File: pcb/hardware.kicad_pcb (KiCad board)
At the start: 4 copper layers, 174 parts, among them J1 Micro_SD_Card_Det_Hirose_DM3AT, J2 USB_A, J3 USB_A, U1 AS4C512M16D3L-12BIN, U2 A33, U3 TPS62095RGTR, U4 TPS62095RGTR, U5 TPS62095RGTR, U6 TPS62095RGTR, U7 AP131-25, U8 MPM-15-5, Y1 24Mhz, Y2 32.768khz

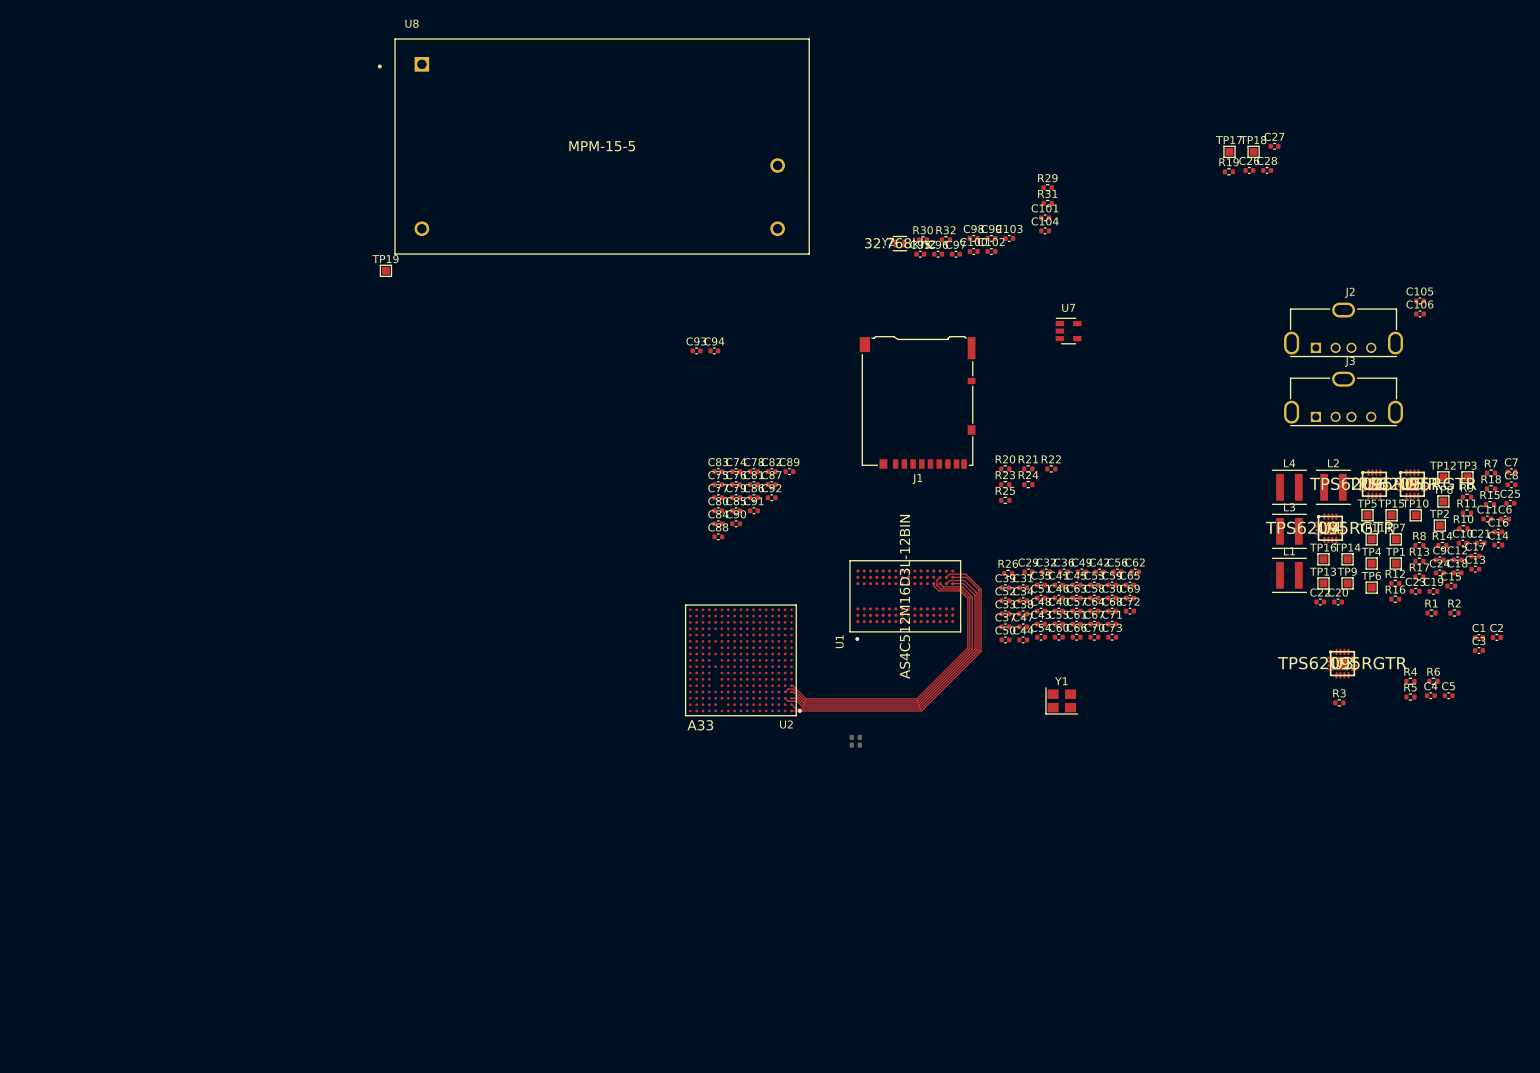
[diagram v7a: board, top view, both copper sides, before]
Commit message: RAM hooked up
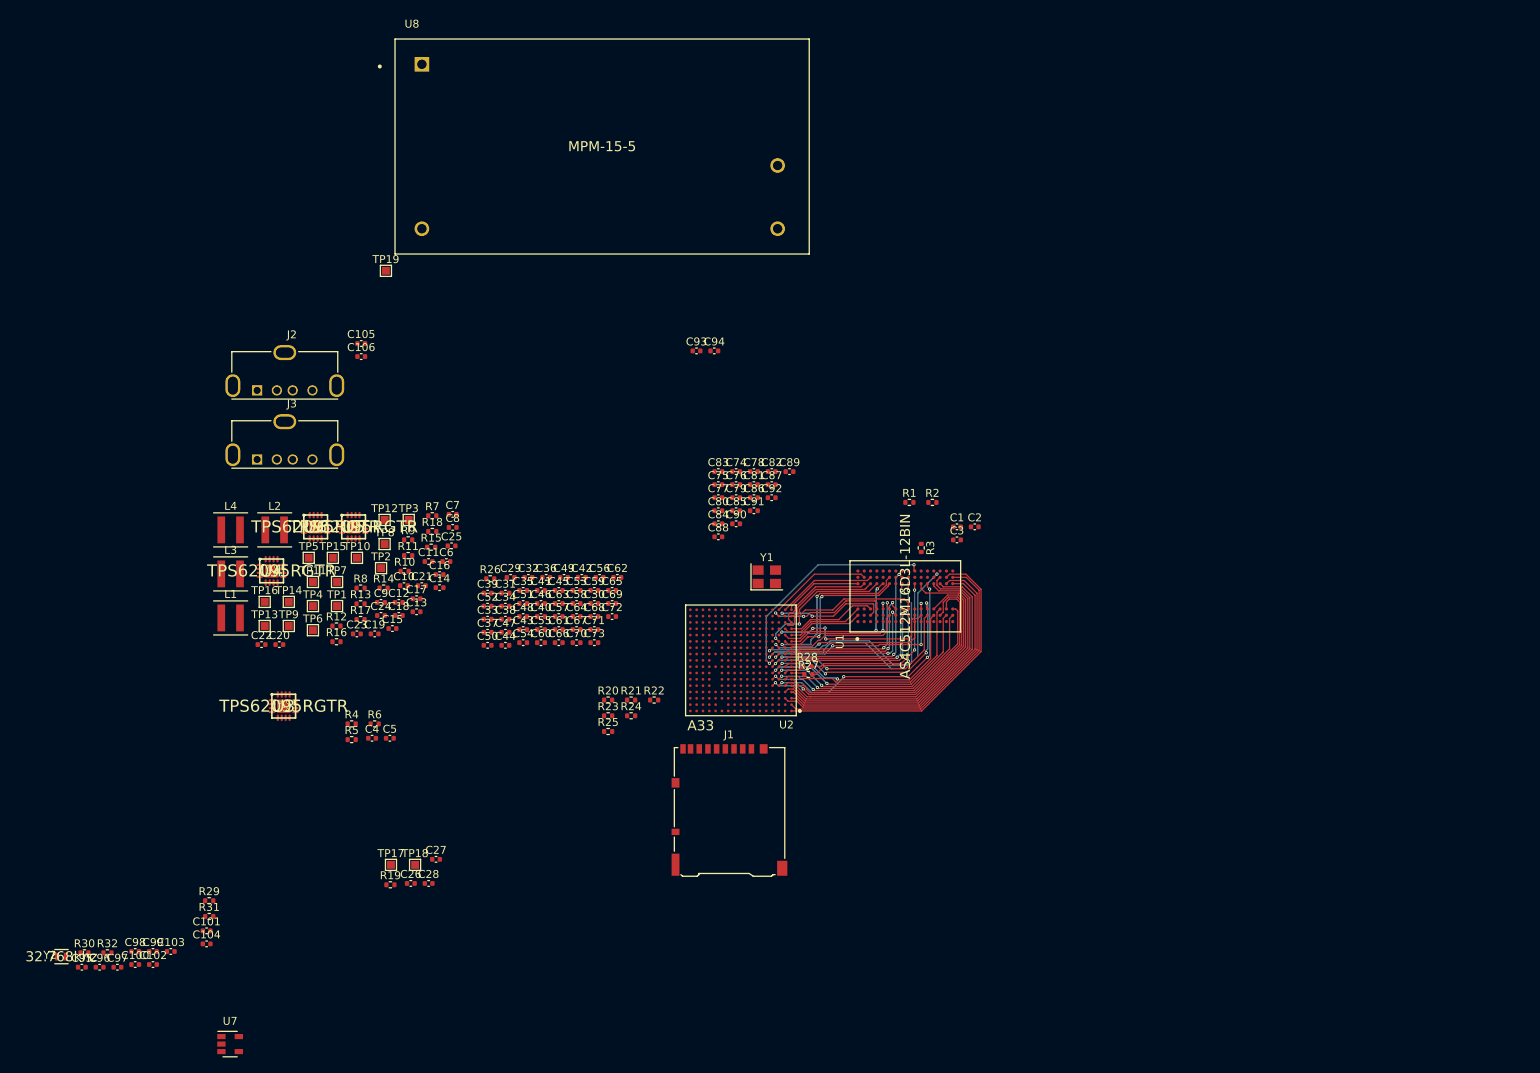
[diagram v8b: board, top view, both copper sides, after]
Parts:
- R27, R28: moved to F.Cu
- moved C100 139.2 mm to (38.1, 147.4)
- moved C101 139.2 mm to (47.2, 143.2)
- moved C102 139.2 mm to (40.4, 147.4)
- moved C103 139.2 mm to (42.6, 145.8)
- moved C104 139.2 mm to (47.2, 144.8)
- moved C27 139.2 mm to (76.2, 134.1)
- moved C95 139.2 mm to (31.4, 147.8)
- moved C96 139.2 mm to (33.6, 147.8)
- moved C97 139.2 mm to (35.9, 147.8)
- moved C98 139.2 mm to (38.1, 145.8)
- moved C99 139.2 mm to (40.4, 145.8)
- moved R19 139.2 mm to (70.4, 137.4)
- moved R29 139.2 mm to (47.5, 139.4)
- moved R30 139.2 mm to (31.7, 146.0)
- moved R31 139.2 mm to (47.5, 141.4)
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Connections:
- U1 pad A7: d12 -> d9
- U1 pad B8: d14 -> d8
- U1 pad C3: d9 -> d14
- U1 pad D7: d8 -> d12
- U2 pad H1: d6 -> d4
- U2 pad J1: d4 -> d5
- U2 pad J2: d5 -> d6
- U2 pad N1: d15 -> d13
- U2 pad P1: d13 -> d14
- U2 pad P2: d14 -> d15
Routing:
- net adr10: track 0.00 -> 39.2 mm
- net adr0: track 0.00 -> 38.1 mm, vias 0 -> 2
- net adr9: track 0.00 -> 35.5 mm, vias 0 -> 2
- net adr5: track 0.00 -> 35.1 mm
- net dba1: track 0.00 -> 32.1 mm, vias 0 -> 2
- net adr15: track 0.00 -> 30.9 mm, vias 0 -> 4
- net adr13: track 0.00 -> 30.7 mm, vias 0 -> 2
- net adr7: track 0.00 -> 29.3 mm, vias 0 -> 2
- net dba2: track 0.00 -> 29.0 mm, vias 0 -> 4
- net /ram/!RST: track 0.00 -> 29.0 mm, vias 0 -> 2
- net /ram/!CKE: track 0.00 -> 28.9 mm, vias 0 -> 2
- net /ram/!CAS: track 0.00 -> 28.1 mm, vias 0 -> 1
- net adr2: track 0.00 -> 27.1 mm
- net adr3: track 0.00 -> 27.0 mm, vias 0 -> 2
- net /ram/!WE: track 0.00 -> 25.6 mm, vias 0 -> 4
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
